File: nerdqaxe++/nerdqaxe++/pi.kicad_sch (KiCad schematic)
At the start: 20 parts, among them J5 Conn_01x12-Socket, J6 Conn_01x12-Socket, J7 Conn_01x12-Header, J8 Conn_01x12-Header, M1 Fan_4pin, M2 Fan_4pin, U30 T-Display-S3, U32 EMC2302-1, U33 TXU0102-DCU, U37 TMP1075, U38 TMP1075

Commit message: DFM
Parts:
- C102, C103, C87, C88, C96: value 100n -> 100nF; footprint Capacitor_SMD:C_0805_2012Metric -> Capacitor_SMD:C_0402_1005Metric
- D3: Manufacturer 1N5819HWQ-7-F -> (none); PARTNO (none) -> 1N5819HWQ-7-F
- J5, J6: Manufacturer 61301211821 -> (none); PARTNO (none) -> 61301211821
- J7, J8: Manufacturer PH1-12-UA -> (none); PARTNO (none) -> PH1-12-UA
- M1, M2: Manufacturer 0470531000 -> (none); PARTNO (none) -> 0470531000
- R33, R35, R36: footprint Resistor_SMD:R_0805_2012Metric -> Resistor_SMD:R_0402_1005Metric
- U32: Manufacturer EMC2302-1-AIZL-TR -> (none); PARTNO (none) -> EMC2302-1-AIZL-TR
- U33: Manufacturer TXU0102DCUR -> (none); PARTNO (none) -> TXU0102DCUR
- U37, U38: Manufacturer TMP1075NDRLR -> (none); PARTNO (none) -> TMP1075NDRLR
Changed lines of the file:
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@@
 			)
 		)
-		(property "Value" "100n"
+		(property "Value" "100nF"
 			(at 254.635 86.995 0)
 			(effects
@@
 			)
 		)
-		(property "Footprint" "Capacitor_SMD:C_0805_2012Metric"
+		(property "Footprint" "Capacitor_SMD:C_0402_1005Metric"
 			(at 253.365 83.185 0)
 			(effects
@@
 			)
 		)
-		(property "Manufacturer" "0470531000"
+		(property "OrderNr" "WM4330-ND"
 			(at 266.065 150.495 0)
 			(effects
@@
 			)
 		)
-		(property "OrderNr" "WM4330-ND"
+		(property "PARTNO" "0470531000"
 			(at 266.065 150.495 0)
 			(effects
@@
 					(size 1.27 1.27)
 				)
-				(hide yes)
 			)
 		)
@@
 			)
 		)
-		(property "Manufacturer" "TMP1075NDRLR"
+		(property "OrderNr" "296-TMP1075NDRLRCT-ND"
 			(at 225.425 56.515 0)
 			(effects
@@
 			)
 		)
-		(property "OrderNr" "296-TMP1075NDRLRCT-ND"
+		(property "PARTNO" "TMP1075NDRLR"
 			(at 225.425 56.515 0)
 			(effects
@@
 					(size 1.27 1.27)
 				)
-				(hide yes)
 			)
 		)
@@
 			)
 		)
-		(property "Value" "100n"
+		(property "Value" "100nF"
 			(at 254.635 59.055 0)
 			(effects
@@
 			)
 		)
-		(property "Footprint" "Capacitor_SMD:C_0805_2012Metric"
+		(property "Footprint" "Capacitor_SMD:C_0402_1005Metric"
 			(at 253.365 55.245 0)
 			(effects
@@
 			)
 		)
-		(property "Value" "100n"
+		(property "Value" "100nF"
 			(at 193.675 109.855 0)
 			(effects
@@
 			)
 		)
-		(property "Footprint" "Capacitor_SMD:C_0805_2012Metric"
+		(property "Footprint" "Capacitor_SMD:C_0402_1005Metric"
 			(at 192.405 106.045 0)
 			(effects
@@
 			)
 		)
-		(property "Footprint" "Resistor_SMD:R_0805_2012Metric"
+		(property "Footprint" "Resistor_SMD:R_0402_1005Metric"
 			(at 257.683 113.665 90)
 			(effects
@@
 			)
 		)
-		(property "Manufacturer" "TMP1075NDRLR"
+		(property "OrderNr" "296-TMP1075NDRLRCT-ND"
 			(at 225.425 84.455 0)
 			(effects
@@
 			)
 		)
-		(property "OrderNr" "296-TMP1075NDRLRCT-ND"
+		(property "PARTNO" "TMP1075NDRLR"
 			(at 225.425 84.455 0)
 			(effects
@@
 					(size 1.27 1.27)
 				)
-				(hide yes)
 			)
 		)
@@
 			)
 		)
-		(property "Manufacturer" "61301211821"
+		(property "OrderNr" "732-61301211821-ND"
 			(at 27.94 190.5 0)
 			(effects
@@
 			)
 		)
-		(property "OrderNr" "732-61301211821-ND"
+		(property "PARTNO" "61301211821"
 			(at 27.94 190.5 0)
 			(effects
@@
 					(size 1.27 1.27)
 				)
-				(hide yes)
 			)
 		)
@@
 			)
 		)
-		(property "Manufacturer" "EMC2302-1-AIZL-TR"
+		(property "OrderNr" "EMC2302-1-AIZL-CT-ND"
 			(at 159.385 139.065 0)
 			(effects
@@
 			)
 		)
-		(property "OrderNr" "EMC2302-1-AIZL-CT-ND"
+		(property "PARTNO" "EMC2302-1-AIZL-TR"
 			(at 159.385 139.065 0)
 			(effects
@@
 					(size 1.27 1.27)
 				)
-				(hide yes)
 			)
 		)
@@
 			)
 		)
-		(property "Manufacturer" "PH1-12-UA"
+		(property "OrderNr" "2057-PH1-12-UA-ND"
 			(at 60.325 190.5 0)
 			(effects
@@
 			)
 		)
-		(property "OrderNr" "2057-PH1-12-UA-ND"
+		(property "PARTNO" "PH1-12-UA"
 			(at 60.325 190.5 0)
 			(effects
@@
 					(size 1.27 1.27)
 				)
-				(hide yes)
 			)
 		)
@@
 			)
 		)
-		(property "Manufacturer" "61301211821"
+		(property "OrderNr" "732-61301211821-ND"
 			(at 27.94 181.61 0)
 			(effects
@@
 			)
 		)
-		(property "OrderNr" "732-61301211821-ND"
+		(property "PARTNO" "61301211821"
 			(at 27.94 181.61 0)
 			(effects
@@
 					(size 1.27 1.27)
 				)
-				(hide yes)
 			)
 		)
@@
 			)
 		)
-		(property "Footprint" "Resistor_SMD:R_0805_2012Metric"
+		(property "Footprint" "Resistor_SMD:R_0402_1005Metric"
 			(at 84.963 75.565 90)
 			(effects
@@
 			)
 		)
-		(property "Manufacturer" "0470531000"
+		(property "OrderNr" "WM4330-ND"
 			(at 266.065 120.015 0)
 			(effects
@@
 			)
 		)
-		(property "OrderNr" "WM4330-ND"
+		(property "PARTNO" "0470531000"
 			(at 266.065 120.015 0)
 			(effects
@@
 					(size 1.27 1.27)
 				)
-				(hide yes)
 			)
 		)
@@
 			)
 		)
-		(property "Value" "100n"
+		(property "Value" "100nF"
 			(at 145.415 165.735 0)
 			(effects
@@
 			)
 		)
-		(property "Footprint" "Capacitor_SMD:C_0805_2012Metric"
+		(property "Footprint" "Capacitor_SMD:C_0402_1005Metric"
 			(at 144.145 161.925 0)
 			(effects
@@
 			)
 		)
-		(property "Manufacturer" "1N5819HWQ-7-F"
+		(property "OrderNr" "31-1N5819HWQ-7-FCT-ND"
 			(at 109.855 99.695 0)
 			(effects
@@
 			)
 		)
-		(property "OrderNr" "31-1N5819HWQ-7-FCT-ND"
+		(property "PARTNO" "1N5819HWQ-7-F"
 			(at 109.855 99.695 0)
 			(effects
@@
 					(size 1.27 1.27)
 				)
-				(hide yes)
 			)
 		)
@@
 			)
 		)
-		(property "Manufacturer" "TXU0102DCUR"
+		(property "OrderNr" "296-TXU0102DCURCT-ND"
 			(at 210.185 133.985 0)
 			(effects
@@
 			)
 		)
-		(property "OrderNr" "296-TXU0102DCURCT-ND"
+		(property "PARTNO" "TXU0102DCUR"
 			(at 210.185 133.985 0)
 			(effects
@@
 					(size 1.27 1.27)
 				)
-				(hide yes)
 			)
 		)
@@
 			)
 		)
-		(property "Footprint" "Resistor_SMD:R_0805_2012Metric"
+		(property "Footprint" "Resistor_SMD:R_0402_1005Metric"
 			(at 257.683 144.145 90)
 			(effects
@@
 			)
 		)
-		(property "Value" "100n"
+		(property "Value" "100nF"
 			(at 201.295 109.855 0)
 			(effects
@@
 			)
 		)
-		(property "Footprint" "Capacitor_SMD:C_0805_2012Metric"
+		(property "Footprint" "Capacitor_SMD:C_0402_1005Metric"
 			(at 200.025 106.045 0)
 			(effects
@@
 			)
 		)
-		(property "Manufacturer" "PH1-12-UA"
+		(property "OrderNr" "2057-PH1-12-UA-ND"
 			(at 60.325 181.61 0)
 			(effects
@@
 			)
 		)
-		(property "OrderNr" "2057-PH1-12-UA-ND"
+		(property "PARTNO" "PH1-12-UA"
 			(at 60.325 181.61 0)
 			(effects
@@
 					(size 1.27 1.27)
 				)
-				(hide yes)
 			)
 		)

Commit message: 5v
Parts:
- C102, C103, C87, C88, C96: PARTNO (none) -> CL05A104KO5NNNC
- R36: PARTNO (none) -> RC0402JR-0710KL
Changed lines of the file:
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@@
 			)
 		)
-		(property "PARTNO" ""
+		(property "PARTNO" "CL05A104KO5NNNC"
 			(at 253.365 83.185 0)
 			(effects
@@
 			)
 		)
-		(property "PARTNO" ""
+		(property "PARTNO" "CL05A104KO5NNNC"
 			(at 253.365 55.245 0)
 			(effects
@@
 			)
 		)
-		(property "PARTNO" ""
+		(property "PARTNO" "CL05A104KO5NNNC"
 			(at 192.405 106.045 0)
 			(effects
@@
 			)
 		)
+		(property "PARTNO" "RC0402JR-0710KL"
+			(at 83.185 75.565 0)
+			(effects
+				(font
+					(size 1.27 1.27)
+				)
+			)
+		)
 		(pin "1"
 		)
@@
 			)
 		)
-		(property "PARTNO" ""
+		(property "PARTNO" "CL05A104KO5NNNC"
 			(at 144.145 161.925 0)
 			(effects
@@
 			)
 		)
-		(property "PARTNO" ""
+		(property "PARTNO" "CL05A104KO5NNNC"
 			(at 200.025 106.045 0)
 			(effects

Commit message: finishing up
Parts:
- C102, C103, C87, C88, C96: LCSC (none) -> C60474; Manufacturer  (none) -> YAGEO; PARTNO CL05A104KO5NNNC -> CC0402KRX7R7BB104
- D3: Manufacturer  (none) -> Diodes Incorporated
- J7, J8: PARTNO PH1-12-UA -> (none)
- R33, R35: LCSC (none) -> C138017; Manufacturer  (none) -> YAGEO; PARTNO (none) -> RC0402FR-072K7L
- R36: LCSC (none) -> C471764; Manufacturer  (none) -> YAGEO; PARTNO RC0402JR-0710KL -> RC0402DR-0710KL
- U32: Manufacturer  (none) -> Microchip Tech
- U33, U37, U38: Manufacturer  (none) -> Texas Instruments

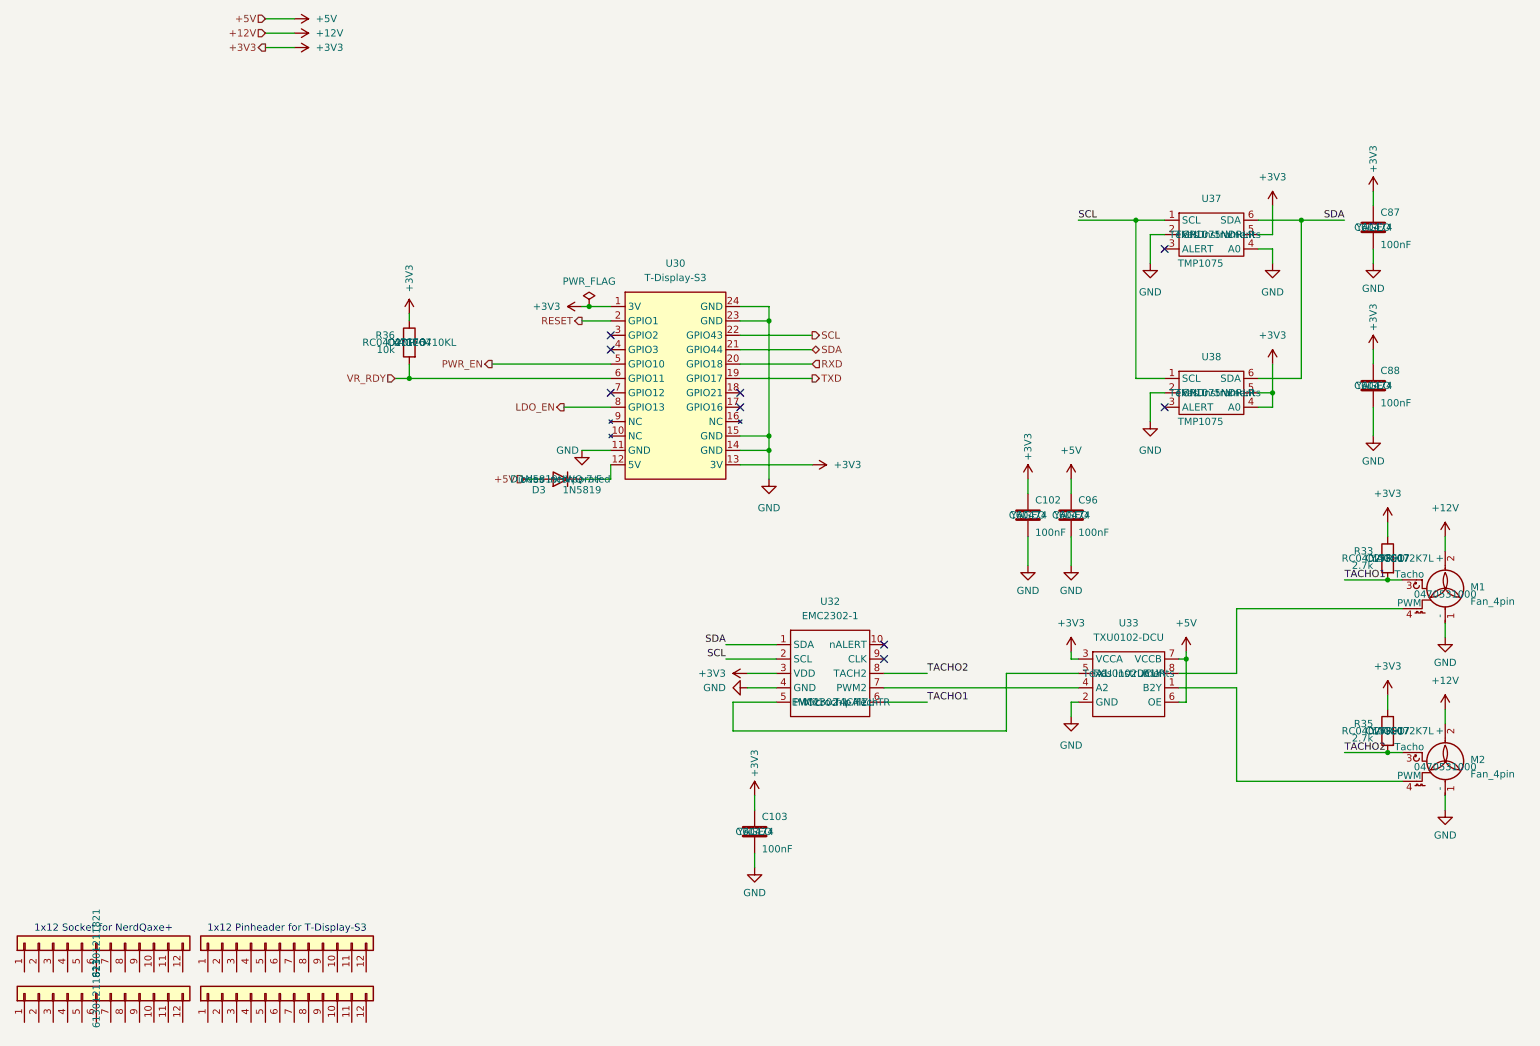
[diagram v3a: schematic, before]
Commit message: hide unnecessary fields in schematic
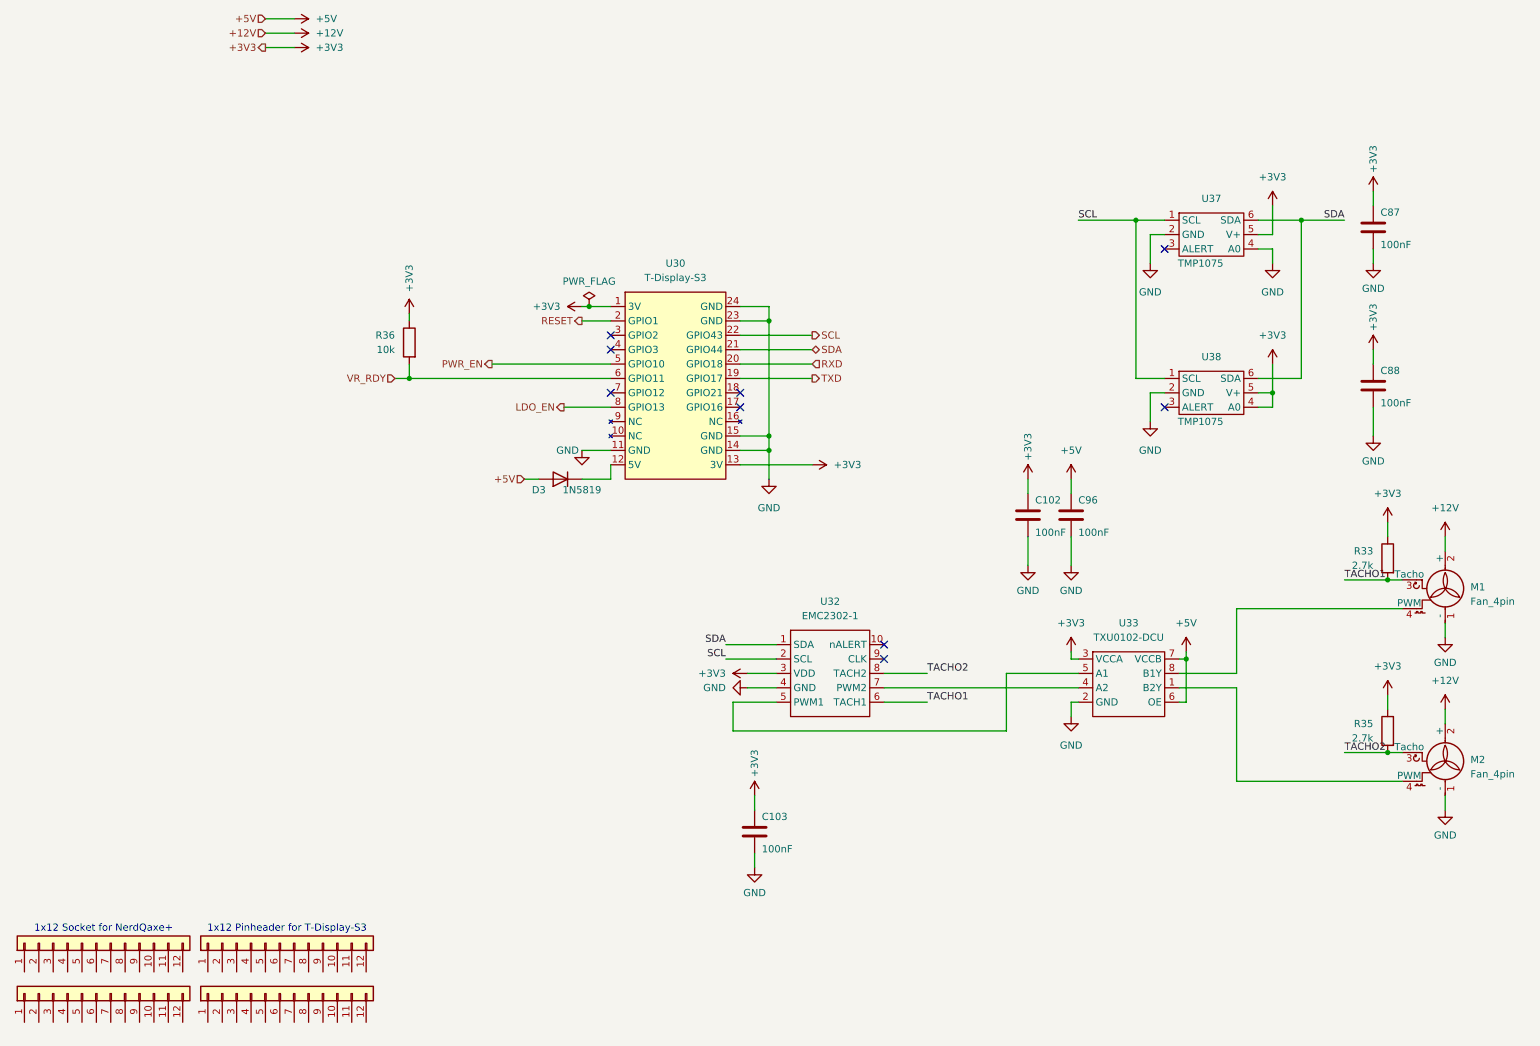
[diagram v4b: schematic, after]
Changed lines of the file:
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@@
 					(size 1.27 1.27)
 				)
+				(hide yes)
 			)
 		)
@@
 					(size 1.27 1.27)
 				)
+				(hide yes)
 			)
 		)
@@
 					(size 1.27 1.27)
 				)
+				(hide yes)
 			)
 		)
@@
 					(size 1.27 1.27)
 				)
+				(hide yes)
 			)
 		)
@@
 					(size 1.27 1.27)
 				)
+				(hide yes)
 			)
 		)
@@
 					(size 1.27 1.27)
 				)
+				(hide yes)
 			)
 		)
@@
 					(size 1.27 1.27)
 				)
+				(hide yes)
 			)
 		)
@@
 					(size 1.27 1.27)
 				)
+				(hide yes)
 			)
 		)
@@
 					(size 1.27 1.27)
 				)
+				(hide yes)
 			)
 		)
@@
 					(size 1.27 1.27)
 				)
+				(hide yes)
 			)
 		)
@@
 					(size 1.27 1.27)
 				)
+				(hide yes)
 			)
 		)
@@
 					(size 1.27 1.27)
 				)
+				(hide yes)
 			)
 		)
@@
 					(size 1.27 1.27)
 				)
+				(hide yes)
 			)
 		)
@@
 					(size 1.27 1.27)
 				)
+				(hide yes)
 			)
 		)
@@
 					(size 1.27 1.27)
 				)
+				(hide yes)
 			)
 		)
@@
 					(size 1.27 1.27)
 				)
+				(hide yes)
 			)
 		)
@@
 					(size 1.27 1.27)
 				)
+				(hide yes)
 			)
 		)
@@
 					(size 1.27 1.27)
 				)
+				(hide yes)
 			)
 		)
@@
 					(size 1.27 1.27)
 				)
+				(hide yes)
 			)
 		)
@@
 					(size 1.27 1.27)
 				)
+				(hide yes)
 			)
 		)
@@
 					(size 1.27 1.27)
 				)
+				(hide yes)
 			)
 		)
@@
 					(size 1.27 1.27)
 				)
+				(hide yes)
 			)
 		)
@@
 					(size 1.27 1.27)
 				)
+				(hide yes)
 			)
 		)
@@
 					(size 1.27 1.27)
 				)
+				(hide yes)
 			)
 		)
@@
 					(size 1.27 1.27)
 				)
+				(hide yes)
 			)
 		)
@@
 					(size 1.27 1.27)
 				)
+				(hide yes)
 			)
 		)
@@
 					(size 1.27 1.27)
 				)
+				(hide yes)
 			)
 		)
@@
 					(size 1.27 1.27)
 				)
+				(hide yes)
 			)
 		)
@@
 					(size 1.27 1.27)
 				)
+				(hide yes)
 			)
 		)
@@
 					(size 1.27 1.27)
 				)
+				(hide yes)
 			)
 		)
@@
 					(size 1.27 1.27)
 				)
+				(hide yes)
 			)
 		)
@@
 					(size 1.27 1.27)
 				)
+				(hide yes)
 			)
 		)
@@
 					(size 1.27 1.27)
 				)
+				(hide yes)
 			)
 		)
@@
 					(size 1.27 1.27)
 				)
+				(hide yes)
 			)
 		)
@@
 					(size 1.27 1.27)
 				)
+				(hide yes)
 			)
 		)
@@
 					(size 1.27 1.27)
 				)
+				(hide yes)
 			)
 		)
@@
 					(size 1.27 1.27)
 				)
+				(hide yes)
 			)
 		)
@@
 					(size 1.27 1.27)
 				)
+				(hide yes)
 			)
 		)
@@
 					(size 1.27 1.27)
 				)
+				(hide yes)
 			)
 		)
@@
 					(size 1.27 1.27)
 				)
+				(hide yes)
 			)
 		)
@@
 					(size 1.27 1.27)
 				)
+				(hide yes)
 			)
 		)
@@
 					(size 1.27 1.27)
 				)
+				(hide yes)
 			)
 		)

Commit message: layout
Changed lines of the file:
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@@
 				)
 				(justify left bottom)
+				(hide yes)
 			)
 		)
@@
 				)
 				(justify left)
+				(hide yes)
 			)
 		)
@@
 					(size 1.27 1.27)
 				)
+				(hide yes)
 			)
 		)
@@
 				)
 				(justify left bottom)
+				(hide yes)
 			)
 		)
@@
 				)
 				(justify left bottom)
+				(hide yes)
 			)
 		)
@@
 				)
 				(justify left)
+				(hide yes)
 			)
 		)
@@
 					(size 1.27 1.27)
 				)
+				(hide yes)
 			)
 		)
@@
 					(size 1.27 1.27)
 				)
+				(hide yes)
 			)
 		)
@@
 					(size 1.27 1.27)
 				)
+				(hide yes)
 			)
 		)
@@
 				)
 				(justify left)
+				(hide yes)
 			)
 		)
@@
 				)
 				(justify left)
+				(hide yes)
 			)
 		)
@@
 				)
 				(justify left bottom)
+				(hide yes)
 			)
 		)
@@
 					(size 1.27 1.27)
 				)
+				(hide yes)
 			)
 		)
@@
 					(size 1.27 1.27)
 				)
+				(hide yes)
 			)
 		)
@@
 				)
 				(justify left)
+				(hide yes)
 			)
 		)
@@
 				)
 				(justify left bottom)
+				(hide yes)
 			)
 		)

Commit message: Rev. 6.1
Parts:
- added R17, R8: 4.7k, Resistor_SMD:R_0402_1005Metric, symbol Device:R
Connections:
- net +3V3: now also R17.2, R8.2
- net SCL: now also R8.1
- net SDA: now also R17.1

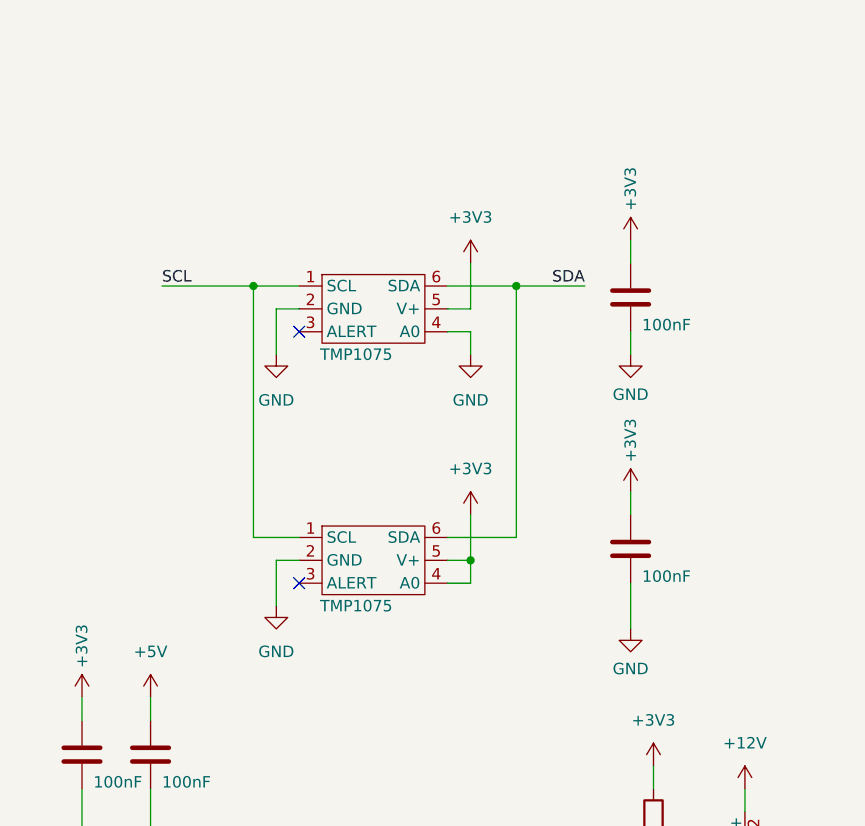
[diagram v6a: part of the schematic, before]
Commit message: clean DRC (incomplete)
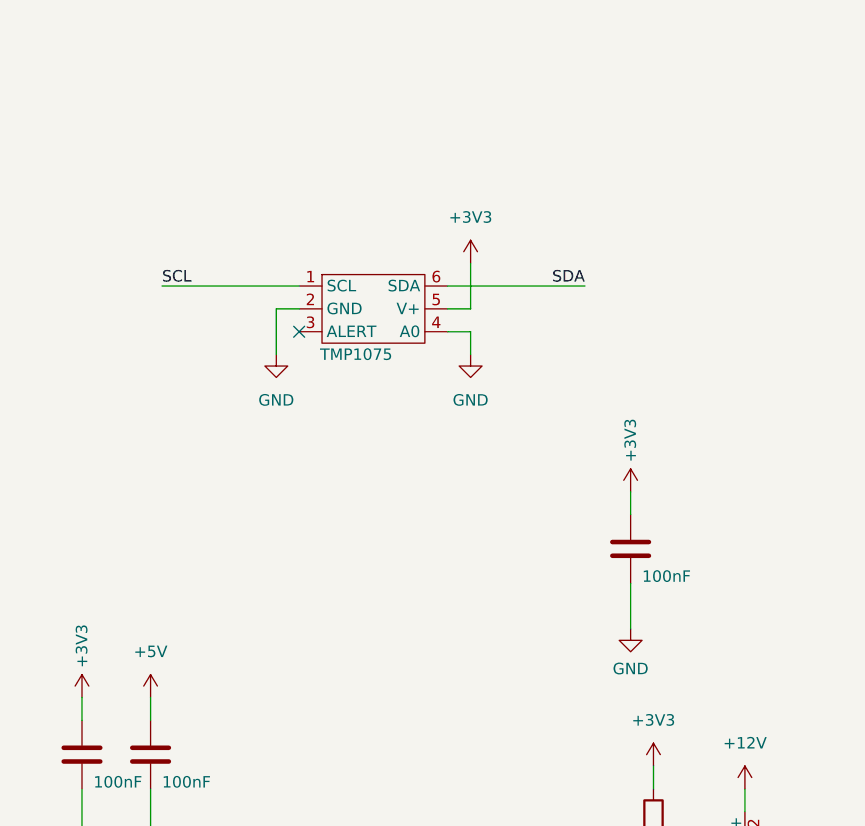
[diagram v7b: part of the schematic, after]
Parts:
- removed C87: 100nF, Capacitor_SMD:C_0402_1005Metric, symbol Device:C
- removed U38: TMP1075, myfootprints:TMP1075-DRL, symbol mylib7:TMP1075-DRL-SOT563
- U37: footprint myfootprints:TMP1075-DRL -> qaxe:TMP1075-DRL
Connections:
- no-connect marks 9 -> 8

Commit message: feature complete
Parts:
- removed R36: 10k, Resistor_SMD:R_0402_1005Metric, symbol Device:R
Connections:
- net SMB_ALRT: now reaches U30.3 (GPIO2)
- net VR_RDY renamed PGOOD
- no-connect marks 8 -> 7
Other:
- moved on the sheet: R17, R8
